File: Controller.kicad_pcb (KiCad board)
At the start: 4 copper layers, 180 x 89 mm, 39 parts, among them J1 I2C1, J10 I2C2, J11 MOTOR0_PWR, J12 MOTOR1_PWR, J13 MOTOR2_PWR, J14 MOTOR3_PWR, J15 MOTOR4_PWR, J16 MOTOR5_PWR, J17 ARM0_ROT, J18 ARM0_GRB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

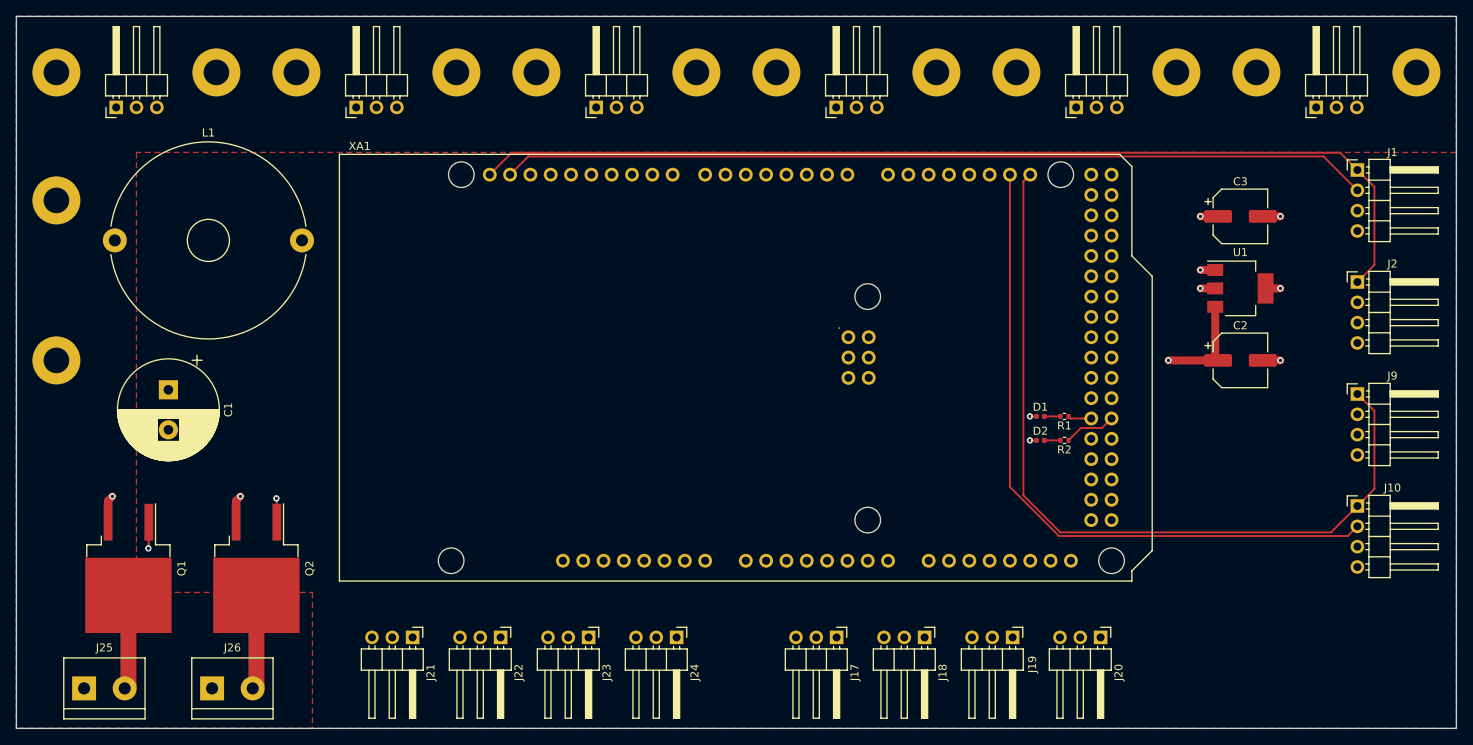
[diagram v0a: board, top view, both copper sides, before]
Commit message: Switch servos to 12V unfiltered rail
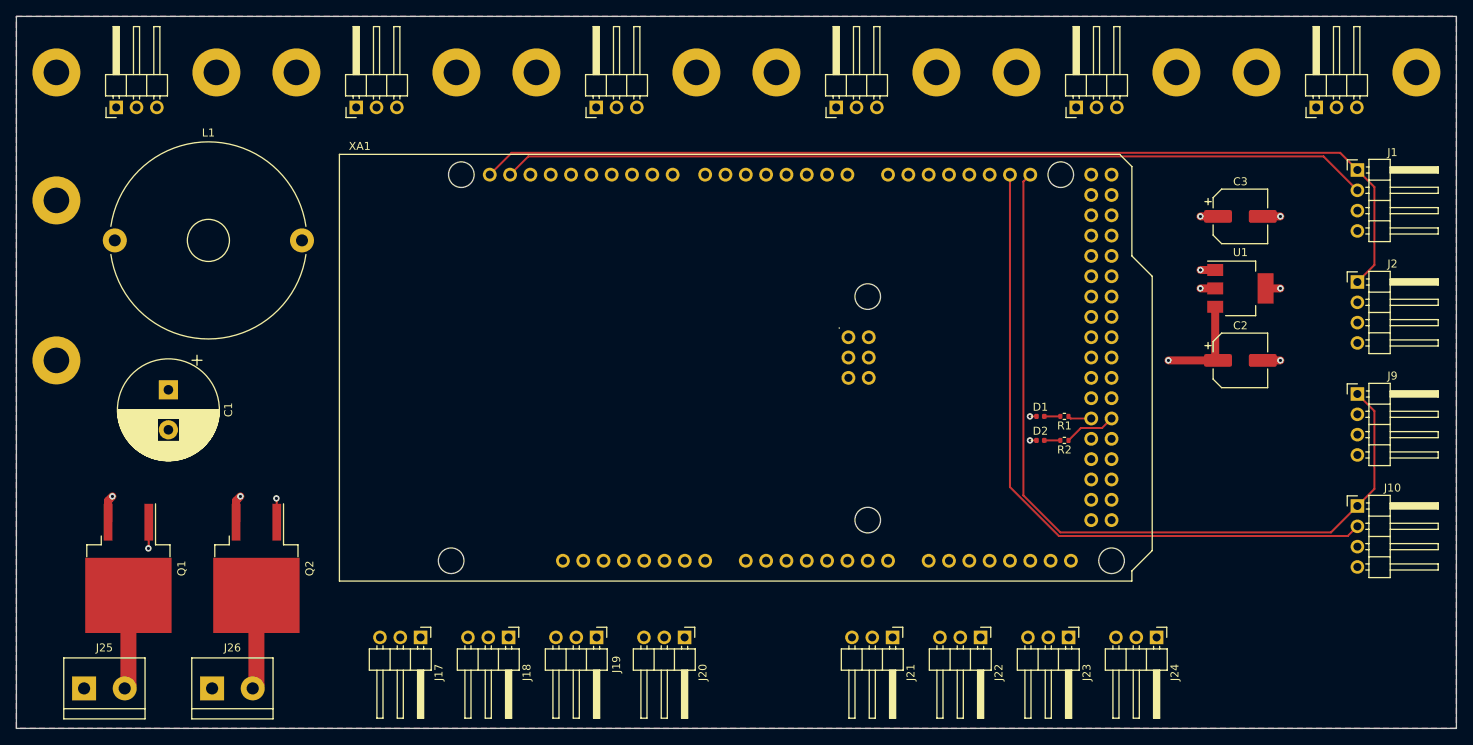
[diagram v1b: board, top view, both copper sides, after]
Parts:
- moved J21 60.0 mm to (150.5, 113.6)
- moved J22 60.0 mm to (161.5, 113.6)
- moved J23 60.0 mm to (172.5, 113.6)
- moved J24 60.0 mm to (183.5, 113.6)
- moved J17 52.0 mm to (91.5, 113.6)
- moved J18 52.0 mm to (102.5, 113.6)
- moved J19 52.0 mm to (113.5, 113.6)
- moved J20 52.0 mm to (124.5, 113.6)
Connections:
- J17 pad 2: +5V -> +12VA
- J18 pad 2: +5V -> +12VA
- J19 pad 2: +5V -> +12VA
- J20 pad 2: +5V -> +12VA
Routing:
- net A3: track 20.2 -> 47.7 mm
- net ARM1_GRB: track 101.8 -> 77.1 mm
- net A0: track 45.6 -> 22.3 mm
- net A2: track 28.7 -> 39.2 mm
- net ARM1_ROT: track 117.7 -> 109.5 mm
- net ARM0_GRB: track 128.8 -> 122.5 mm
- net A1: track 37.2 -> 31.0 mm
- net ARM0_ROT: track 140.0 -> 135.4 mm

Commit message: Decrease board size to 80mm wide
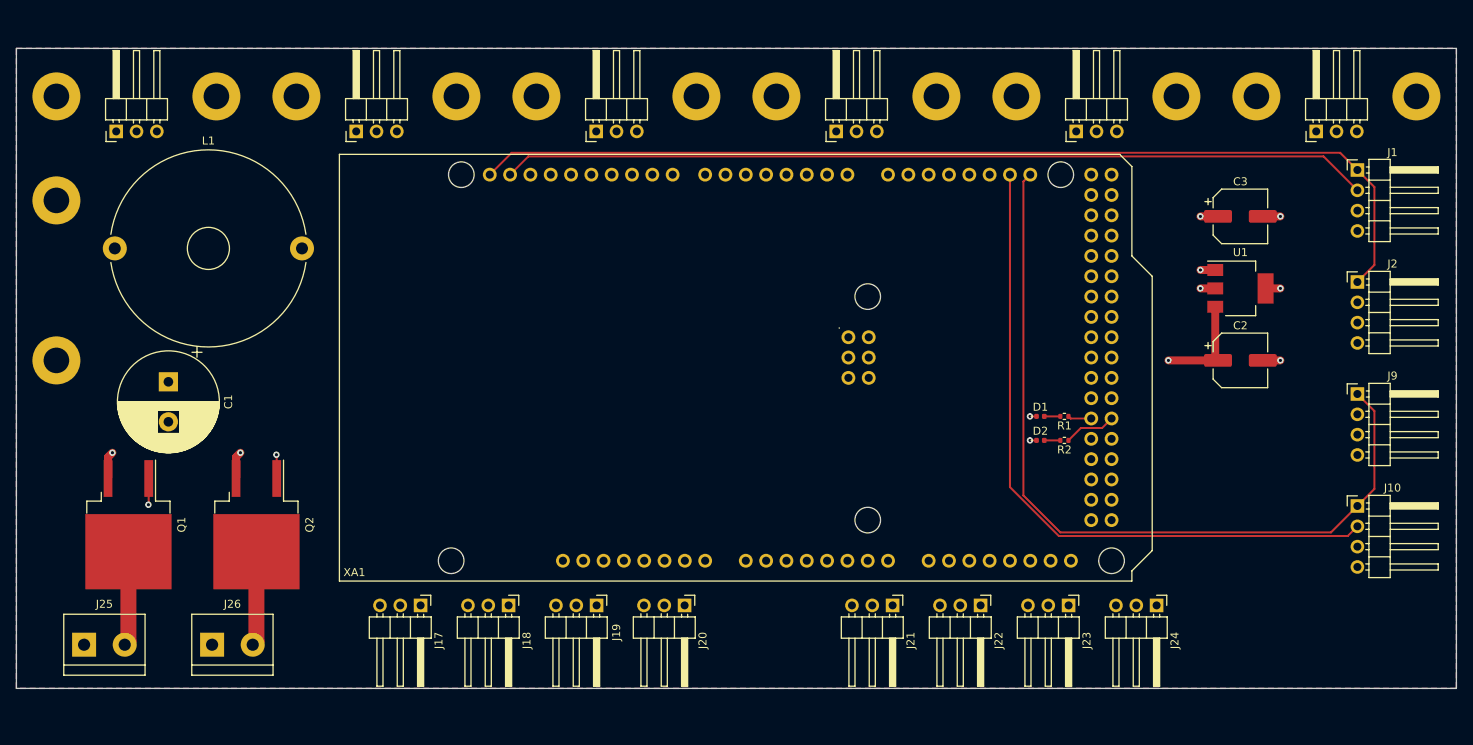
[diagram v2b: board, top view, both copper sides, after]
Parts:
- moved J25 5.46 mm to (49.5, 114.5)
- moved J26 5.46 mm to (65.5, 114.5)
- moved Q1 5.46 mm to (55.0, 99.5)
- moved Q2 5.46 mm to (71.0, 99.5)
- moved J17 4.00 mm to (91.5, 109.6)
- moved J18 4.00 mm to (102.5, 109.6)
- moved J19 4.00 mm to (113.5, 109.6)
- moved J20 4.00 mm to (124.5, 109.6)
- moved J21 4.00 mm to (150.5, 109.6)
- moved J22 4.00 mm to (161.5, 109.6)
- moved J23 4.00 mm to (172.5, 109.6)
- moved J24 4.00 mm to (183.5, 109.6)
- moved J11 3.00 mm to (206.0, 46.0)
- moved J12 3.00 mm to (176.0, 46.0)
- moved J13 3.00 mm to (146.0, 46.0)
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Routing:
- net ARM0_ROT: track 135.4 -> 100.0 mm
- net ARM0_GRB: track 122.5 -> 88.9 mm
- net ARM1_ROT: track 109.5 -> 77.9 mm
- net ARM1_GRB: track 77.1 -> 63.9 mm
- net LED1: track 58.7 -> 62.3 mm
- net LED0: track 86.9 -> 83.7 mm
- net A1: track 31.0 -> 29.1 mm
- net A0: track 22.3 -> 20.7 mm
- net A3: track 47.7 -> 46.0 mm
- net A2: track 39.2 -> 37.6 mm
- net MOTOR3: track 22.4 -> 20.9 mm
- net MOTOR5: track 77.1 -> 75.9 mm
- net MOTOR4: track 49.6 -> 48.4 mm
- net MOTOR0: track 67.2 -> 65.9 mm
- net MOTOR1: track 39.7 -> 38.5 mm
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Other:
- board size 180 x 89 mm -> 180 x 80 mm

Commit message: Add silkscreen labels
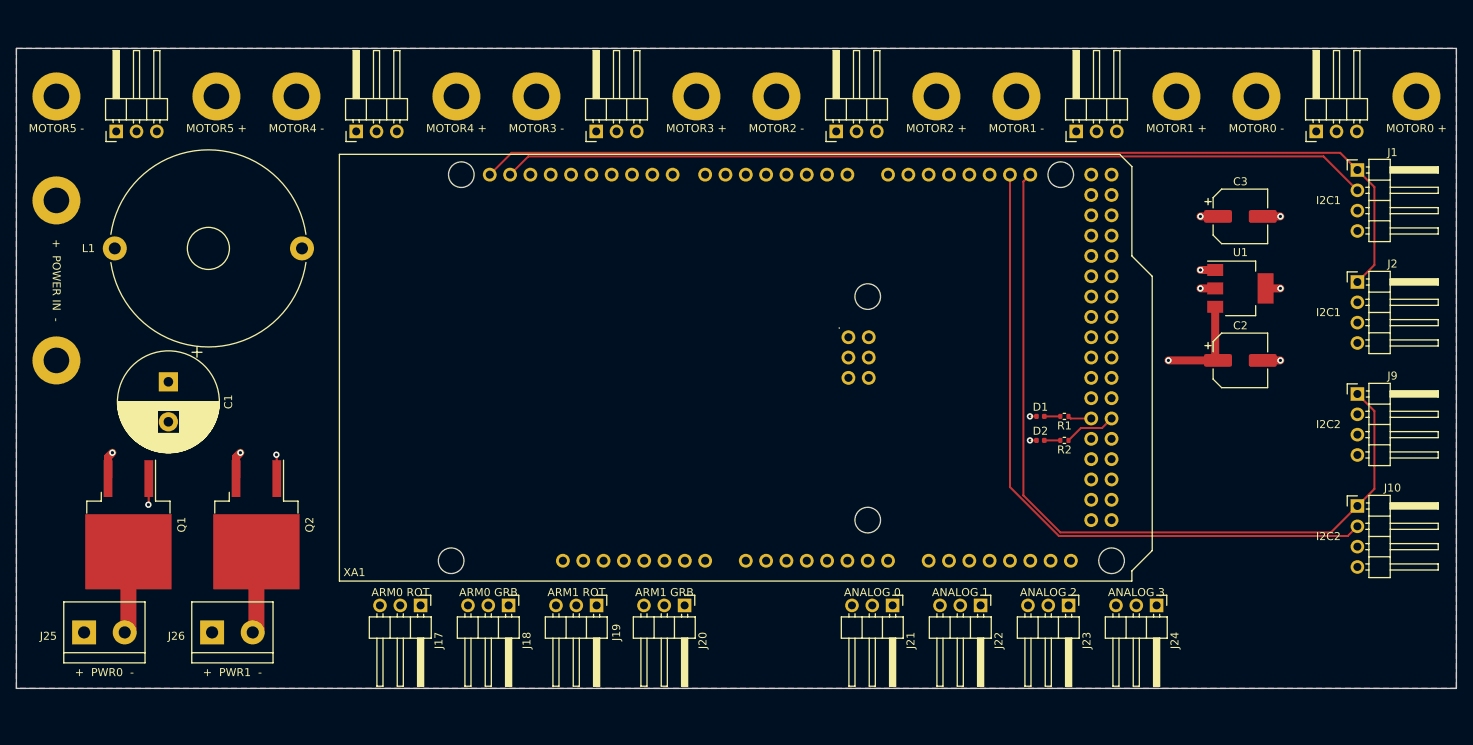
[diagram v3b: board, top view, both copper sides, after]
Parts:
- moved J25 1.54 mm to (49.5, 113.0)
- moved J26 1.54 mm to (65.5, 113.0)
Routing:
- net Net-(J26-Pad2): track 11.8 -> 10.3 mm
- net Net-(J25-Pad2): track 11.8 -> 10.3 mm
- net +12VA: track 0.54 -> 0.00 mm
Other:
- board text added: "+ POWER IN -"
- board text added: "+ PWR0 -"
- board text added: "+ PWR1 -"
- board text added: "ANALOG 0"
- board text added: "ANALOG 1"
- board text added: "ANALOG 2"
- board text added: "ANALOG 3"
- board text added: "ARM0 GRB"
- board text added: "ARM0 ROT"
- board text added: "ARM1 GRB"
- board text added: "ARM1 ROT"
- board text added: "I2C1"
- board text added: "I2C2"
- board text added: "MOTOR0 +"
- board text added: "MOTOR0 -"
- board text added: "MOTOR1 +"
- board text added: "MOTOR1 -"
- board text added: "MOTOR2 +"
- board text added: "MOTOR2 -"
- board text added: "MOTOR3 +"
- board text added: "MOTOR3 -"
- board text added: "MOTOR4 +"
- board text added: "MOTOR4 -"
- board text added: "MOTOR5 +"
- board text added: "MOTOR5 -"
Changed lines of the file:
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@@
   )
   (footprint "TerminalBlock:TerminalBlock_bornier-2_P5.08mm" (layer "F.Cu")
-    (at 49.46 114.54)
+    (at 49.46 113)
     (descr "simple 2-pin terminal block, pitch 5.08mm, revamped version of bornier2")
     (tags "terminal block bornier2")
@@
     (property "Sheetname" "")
     (attr through_hole)
-    (fp_text reference "J25" (at 2.54 -5.08) (layer "F.SilkS")
+    (fp_text reference "J25" (at -4.46 0.46) (layer "F.SilkS")
       (effects (font (size 1 1) (thickness 0.15)))
     )
@@
   )
   (footprint "TerminalBlock:TerminalBlock_bornier-2_P5.08mm" (layer "F.Cu")
-    (at 65.46 114.54)
+    (at 65.46 113)
     (descr "simple 2-pin terminal block, pitch 5.08mm, revamped version of bornier2")
     (tags "terminal block bornier2")
@@
     (property "Sheetname" "")
     (attr through_hole)
-    (fp_text reference "J26" (at 2.54 -5.08) (layer "F.SilkS")
+    (fp_text reference "J26" (at -4.46 0.46) (layer "F.SilkS")
       (effects (font (size 1 1) (thickness 0.15)))
     )
@@
     (property "Sheetname" "")
     (attr through_hole)
-    (fp_text reference "L1" (at 11.7 -13.45) (layer "F.SilkS")
+    (fp_text reference "L1" (at -3.3 0) (layer "F.SilkS")
       (effects (font (size 1 1) (thickness 0.15)))
     )
@@
   )
   (gr_rect (start 41 40) (end 221 120) (layer "Edge.Cuts") (width 0.1) (fill none))
+  (gr_text "MOTOR3 -" (at 106 50) (layer "F.SilkS")
+    (effects (font (size 1 1) (thickness 0.15)))
+  )
+  (gr_text "I2C1" (at 205 73) (layer "F.SilkS")
+    (effects (font (size 1 1) (thickness 0.15)))
+  )
+  (gr_text "MOTOR2 +" (at 156 50) (layer "F.SilkS")
+    (effects (font (size 1 1) (thickness 0.15)))
+  )
+  (gr_text "ARM1 ROT" (at 111 108) (layer "F.SilkS")
+    (effects (font (size 1 1) (thickness 0.15)))
+  )
+  (gr_text "ANALOG 3" (at 181 108) (layer "F.SilkS")
+    (effects (font (size 1 1) (thickness 0.15)))
+  )
+  (gr_text "MOTOR5 +" (at 66 50) (layer "F.SilkS")
+    (effects (font (size 1 1) (thickness 0.15)))
+  )
+  (gr_text "ARM0 ROT" (at 89 108) (layer "F.SilkS")
+    (effects (font (size 1 1) (thickness 0.15)))
+  )
+  (gr_text "MOTOR4 -" (at 76 50) (layer "F.SilkS")
+    (effects (font (size 1 1) (thickness 0.15)))
+  )
+  (gr_text "MOTOR3 +" (at 126 50) (layer "F.SilkS")
+    (effects (font (size 1 1) (thickness 0.15)))
+  )
+  (gr_text "MOTOR1 -" (at 166 50) (layer "F.SilkS")
+    (effects (font (size 1 1) (thickness 0.15)))
+  )
+  (gr_text "ANALOG 1" (at 159 108) (layer "F.SilkS")
+    (effects (font (size 1 1) (thickness 0.15)))
+  )
+  (gr_text "+  PWR1  -" (at 68 118) (layer "F.SilkS")
+    (effects (font (size 1 1) (thickness 0.15)))
+  )
+  (gr_text "ARM1 GRB" (at 122 108) (layer "F.SilkS")
+    (effects (font (size 1 1) (thickness 0.15)))
+  )
+  (gr_text "MOTOR1 +" (at 186 50) (layer "F.SilkS")
+    (effects (font (size 1 1) (thickness 0.15)))
+  )
+  (gr_text "MOTOR2 -" (at 136 50) (layer "F.SilkS")
+    (effects (font (size 1 1) (thickness 0.15)))
+  )
+  (gr_text "ANALOG 0" (at 148 108) (layer "F.SilkS")
+    (effects (font (size 1 1) (thickness 0.15)))
+  )
+  (gr_text "+  POWER IN  -" (at 46 69 270) (layer "F.SilkS")
+    (effects (font (size 1 1) (thickness 0.15)))
+  )
+  (gr_text "MOTOR0 +" (at 216 50) (layer "F.SilkS")
+    (effects (font (size 1 1) (thickness 0.15)))
+  )
+  (gr_text "MOTOR4 +" (at 96 50) (layer "F.SilkS")
+    (effects (font (size 1 1) (thickness 0.15)))
+  )
+  (gr_text "ANALOG 2" (at 170 108) (layer "F.SilkS")
+    (effects (font (size 1 1) (thickness 0.15)))
+  )
+  (gr_text "ARM0 GRB" (at 100 108) (layer "F.SilkS")
+    (effects (font (size 1 1) (thickness 0.15)))
+  )
+  (gr_text "I2C1" (at 205 59) (layer "F.SilkS")
+    (effects (font (size 1 1) (thickness 0.15)))
+  )
+  (gr_text "+  PWR0  -" (at 52 118) (layer "F.SilkS")
+    (effects (font (size 1 1) (thickness 0.15)))
+  )
+  (gr_text "MOTOR0 -" (at 196 50) (layer "F.SilkS")
+    (effects (font (size 1 1) (thickness 0.15)))
+  )
+  (gr_text "I2C2" (at 205 87) (layer "F.SilkS")
+    (effects (font (size 1 1) (thickness 0.15)))
+  )
+  (gr_text "MOTOR5 -" (at 46 50) (layer "F.SilkS")
+    (effects (font (size 1 1) (thickness 0.15)))
+  )
+  (gr_text "I2C2" (at 205 101) (layer "F.SilkS")
+    (effects (font (size 1 1) (thickness 0.15)))
+  )
   (segment (start 191.2 79) (end 185 79) (width 1) (layer "F.Cu") (net 1))
   (segment (start 190.85 72.3) (end 190.85 78.65) (width 1) (layer "F.Cu") (net 1))
@@
   (segment (start 208.625 99.74) (end 210.75 97.615) (width 0.25) (layer "In1.Cu") (net 21))
   (segment (start 210.75 87.865) (end 208.625 85.74) (width 0.25) (layer "In1.Cu") (net 21))
-  (segment (start 65.46 114.54) (end 65.46 114) (width 2) (layer "In2.Cu") (net 22))
   (segment (start 127.75 113.5) (end 130.75 110.5) (width 0.25) (layer "In1.Cu") (net 23))
   (segment (start 130.75 110.5) (end 130.75 63.5015) (width 0.25) (layer "In1.Cu") (net 23))
@@
   (segment (start 142.0025 106.25) (end 139.795 104.0425) (width 0.25) (layer "In1.Cu") (net 30))
   (segment (start 180.15 106.25) (end 142.0025 106.25) (width 0.25) (layer "In1.Cu") (net 30))
-  (segment (start 55 102.915) (end 55 114.08) (width 2) (layer "F.Cu") (net 31))
-  (segment (start 55 114.08) (end 54.54 114.54) (width 2) (layer "F.Cu") (net 31))
-  (segment (start 71 102.915) (end 71 114.08) (width 2) (layer "F.Cu") (net 32))
-  (segment (start 71 114.08) (end 70.54 114.54) (width 2) (layer "F.Cu") (net 32))
+  (segment (start 55 102.915) (end 55 112.54) (width 2) (layer "F.Cu") (net 31))
+  (segment (start 55 112.54) (end 54.54 113) (width 2) (layer "F.Cu") (net 31))
+  (segment (start 71 102.915) (end 71 112.54) (width 2) (layer "F.Cu") (net 32))
+  (segment (start 71 112.54) (end 70.54 113) (width 2) (layer "F.Cu") (net 32))
   (segment (start 57.5 97.04) (end 57.54 97) (width 0.25) (layer "F.Cu") (net 33))
   (segment (start 57.54 97) (end 57.54 93.765) (width 0.25) (layer "F.Cu") (net 33))
